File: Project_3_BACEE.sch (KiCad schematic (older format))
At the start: 13 parts, among them U1 24LC1025, U2 24LC1025, U3 DS1337S+, U4 ATMEGA328P-AU, Y1 Crystal 32 MHz, Y2 Crystal 16 MHz

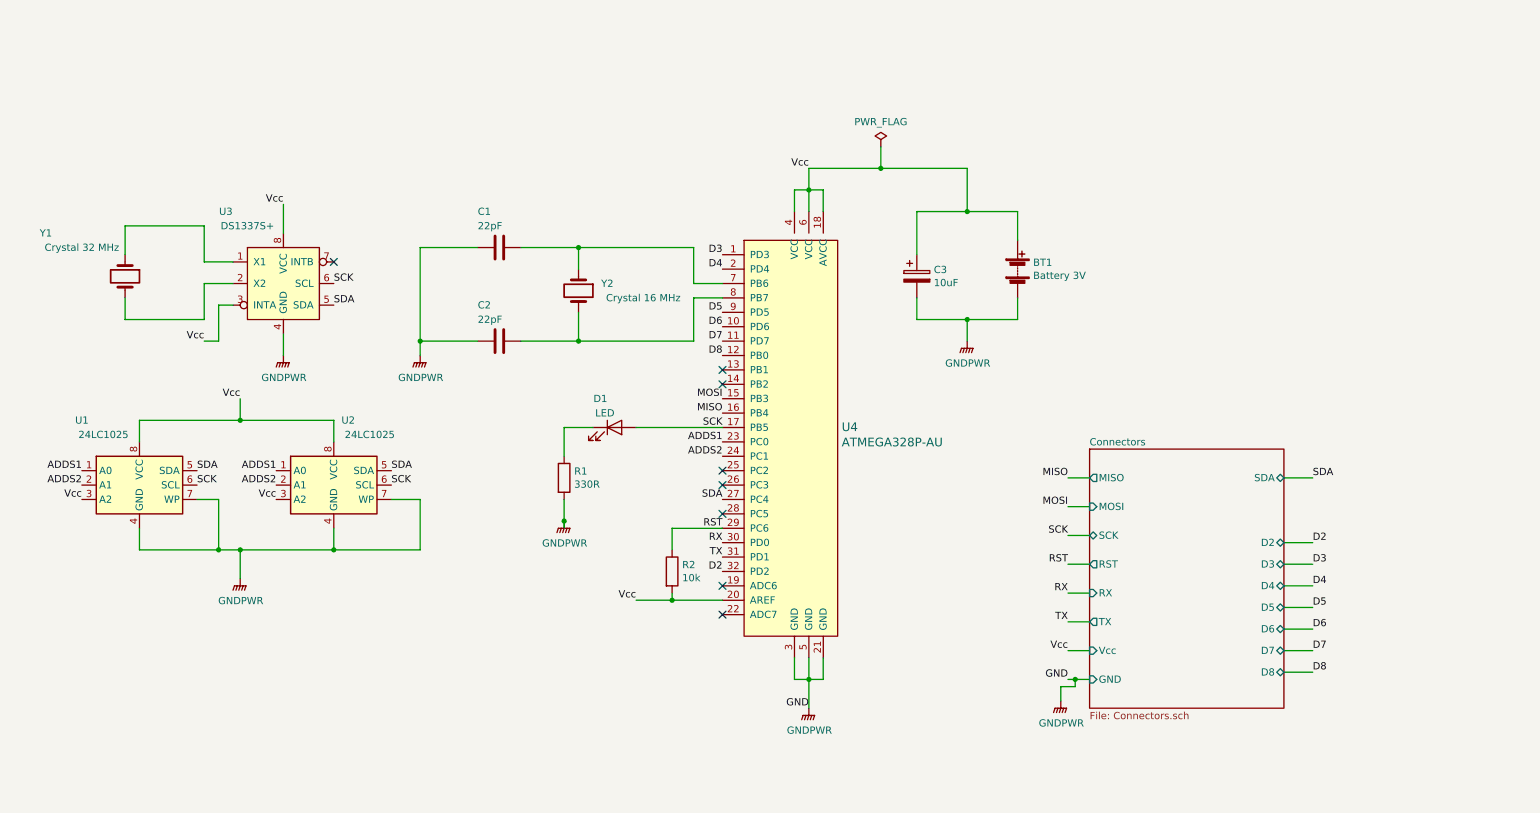
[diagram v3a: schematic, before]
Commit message: Added functional block description.
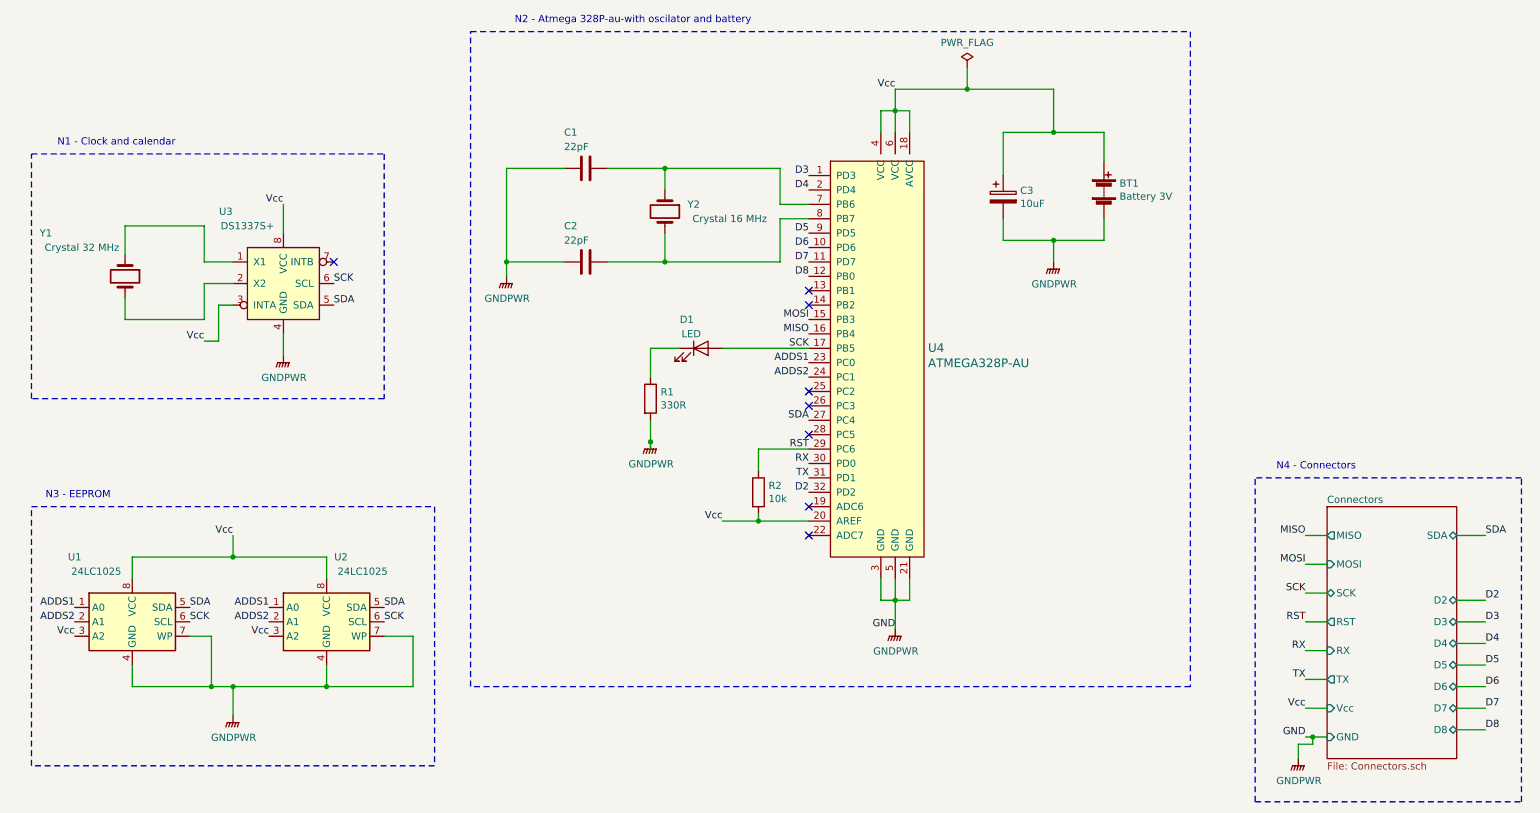
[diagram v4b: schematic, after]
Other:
- note added: "N1 - Clock and calendar"
- note added: "N2 - Atmega 328P-au-with oscilator and battery"
- note added: "N3 - EEPROM"
- note added: "N4 - Connectors"
- moved on the sheet: BT1, C1, C2, C3, D1, R1, R2, U1, U2, U4, Y2
